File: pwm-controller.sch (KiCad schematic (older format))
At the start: 35 parts, among them J1 DEBUG_ADDRESS_I2C_INT, J2 POWER, J3 OUT+, J4 OUT-, SW1 EC12D1524403, U1 STM8S003F3Px, U2 78L05

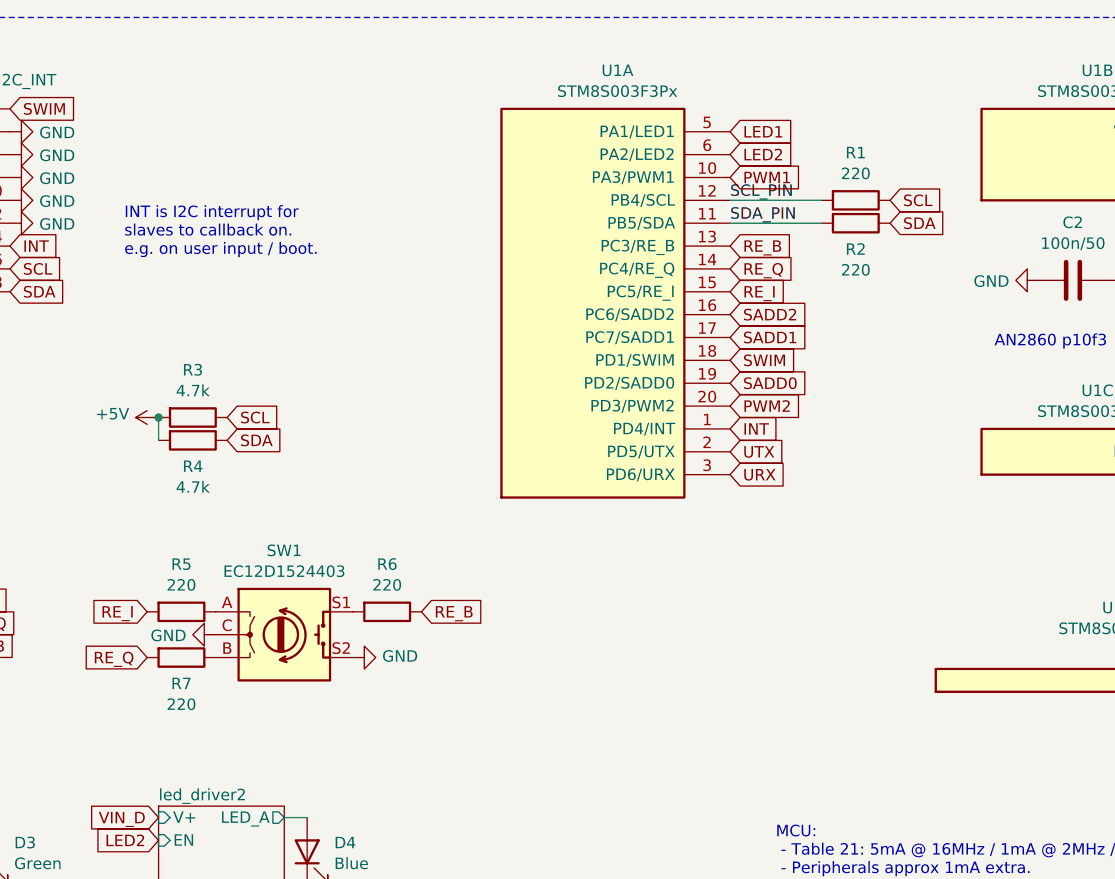
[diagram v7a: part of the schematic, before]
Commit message: add mosfets, fix led+i2c resistors
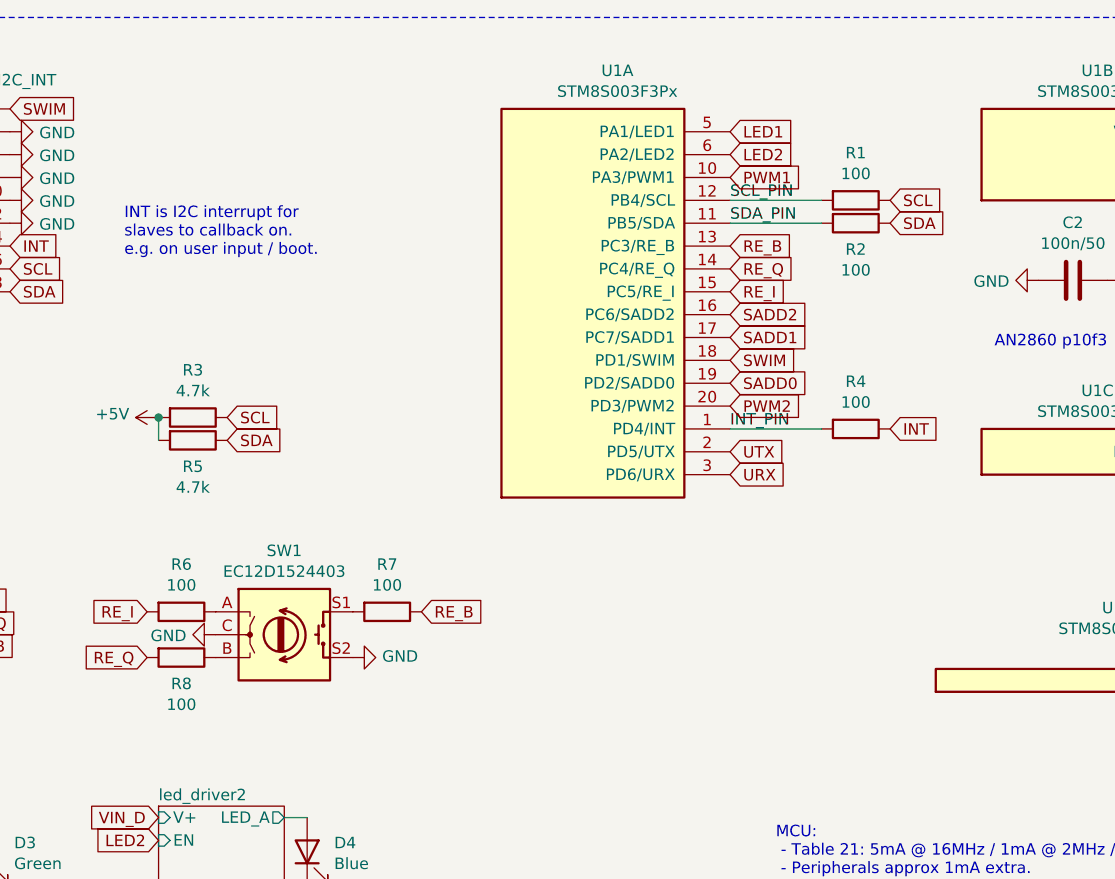
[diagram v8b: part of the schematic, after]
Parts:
- added R4: 100, Resistor_SMD:R_0402_1005Metric, symbol Device:R
- R1, R2: value 220 -> 100; JLC C25091 -> C25076
- R6: renamed from R5; value 220 -> 100; JLC C25091 -> C25076
- R7: renamed from R6; value 220 -> 100; JLC C25091 -> C25076
- R8: renamed from R7; value 220 -> 100; JLC C25091 -> C25076
- TP1: JLC (none) -> -
- renumbered R4 to R5
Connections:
- net INT: now also R4.1; no longer U1.1 (PD4/INT)
- new net INT_PIN: R4.2, U1.1 (PD4/INT)
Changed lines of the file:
@@
 AR Path="/61C031A1/61BB9F0D" Ref="R?"  Part="1"
 AR Path="/61C031A3/61BB9F0D" Ref="R?"  Part="1"
-AR Path="/61BB9F0D" Ref="R4"  Part="1"
-F 0 "R4" V 5915 3650 50  0000 C CNN
+AR Path="/61BB9F0D" Ref="R5"  Part="1"
+F 0 "R5" V 5915 3650 50  0000 C CNN
 F 1 "4.7k" V 6006 3650 50  0000 C CNN
 F 2 "Resistor_SMD:R_0402_1005Metric" V 5730 3650 50  0001 C CNN
@@
 Wire Wire Line
 	6200 6650 6200 6750
-Text GLabel 8150 3600 2    50   Input ~ 0
+Text GLabel 8850 3600 2    50   Input ~ 0
 INT
 Text GLabel 5000 2800 2    50   Input ~ 0
@@
 AR Path="/61C031A1/61CD939B" Ref="R?"  Part="1"
 AR Path="/61C031A3/61CD939B" Ref="R?"  Part="1"
-AR Path="/61CD939B" Ref="R5"  Part="1"
-F 0 "R5" V 5543 4400 50  0000 C CNN
-F 1 "220" V 5634 4400 50  0000 C CNN
+AR Path="/61CD939B" Ref="R6"  Part="1"
+F 0 "R6" V 5543 4400 50  0000 C CNN
+F 1 "100" V 5634 4400 50  0000 C CNN
 F 2 "Resistor_SMD:R_0402_1005Metric" V 5680 4400 50  0001 C CNN
 F 3 "~" H 5750 4400 50  0001 C CNN
-F 4 "C25091" H 5750 4400 50  0001 C CNN "JLC"
+F 4 "C25076" H 5750 4400 50  0001 C CNN "JLC"
 	1    5750 4400
 	0    1    1    0
@@
 AR Path="/61C031A1/61CD98C2" Ref="R?"  Part="1"
 AR Path="/61C031A3/61CD98C2" Ref="R?"  Part="1"
-AR Path="/61CD98C2" Ref="R7"  Part="1"
-F 0 "R7" V 5865 4600 50  0000 C CNN
-F 1 "220" V 5956 4600 50  0000 C CNN
+AR Path="/61CD98C2" Ref="R8"  Part="1"
+F 0 "R8" V 5865 4600 50  0000 C CNN
+F 1 "100" V 5956 4600 50  0000 C CNN
 F 2 "Resistor_SMD:R_0402_1005Metric" V 5680 4600 50  0001 C CNN
 F 3 "~" H 5750 4600 50  0001 C CNN
-F 4 "C25091" H 5750 4600 50  0001 C CNN "JLC"
+F 4 "C25076" H 5750 4600 50  0001 C CNN "JLC"
 	1    5750 4600
 	0    1    1    0
@@
 AR Path="/61C031A1/61CDA382" Ref="R?"  Part="1"
 AR Path="/61C031A3/61CDA382" Ref="R?"  Part="1"
-AR Path="/61CDA382" Ref="R6"  Part="1"
-F 0 "R6" V 6443 4400 50  0000 C CNN
-F 1 "220" V 6534 4400 50  0000 C CNN
+AR Path="/61CDA382" Ref="R7"  Part="1"
+F 0 "R7" V 6443 4400 50  0000 C CNN
+F 1 "100" V 6534 4400 50  0000 C CNN
 F 2 "Resistor_SMD:R_0402_1005Metric" V 6580 4400 50  0001 C CNN
 F 3 "~" H 6650 4400 50  0001 C CNN
-F 4 "C25091" H 6650 4400 50  0001 C CNN "JLC"
+F 4 "C25076" H 6650 4400 50  0001 C CNN "JLC"
 	1    6650 4400
 	0    1    1    0
@@
 AR Path="/61DB5806" Ref="R2"  Part="1"
 F 0 "R2" V 8815 2700 50  0000 C CNN
-F 1 "220" V 8906 2700 50  0000 C CNN
+F 1 "100" V 8906 2700 50  0000 C CNN
 F 2 "Resistor_SMD:R_0402_1005Metric" V 8630 2700 50  0001 C CNN
 F 3 "~" H 8700 2700 50  0001 C CNN
-F 4 "C25091" H 8700 2700 50  0001 C CNN "JLC"
+F 4 "C25076" H 8700 2700 50  0001 C CNN "JLC"
 	1    8700 2700
 	0    1    1    0
@@
 AR Path="/61DB4527" Ref="R1"  Part="1"
 F 0 "R1" V 8493 2600 50  0000 C CNN
-F 1 "220" V 8584 2600 50  0000 C CNN
+F 1 "100" V 8584 2600 50  0000 C CNN
 F 2 "Resistor_SMD:R_0402_1005Metric" V 8630 2600 50  0001 C CNN
 F 3 "~" H 8700 2600 50  0001 C CNN
-F 4 "C25091" H 8700 2600 50  0001 C CNN "JLC"
+F 4 "C25076" H 8700 2600 50  0001 C CNN "JLC"
 	1    8700 2600
 	0    1    1    0
@@
 F 2 "TestPoint:TestPoint_THTPad_D1.5mm_Drill0.7mm" H 2500 5300 50  0001 C CNN
 F 3 "~" H 2500 5300 50  0001 C CNN
+F 4 "-" H 2300 5300 50  0001 C CNN "JLC"
 	1    2300 5300
 	-1   0    0    1
 $EndComp
+$Comp
+L Device:R R?
+U 1 1 62317A5E
+P 8700 3600
+AR Path="/61B5C5B6/62317A5E" Ref="R?"  Part="1"
+AR Path="/61C03040/62317A5E" Ref="R?"  Part="1"
+AR Path="/61C031A1/62317A5E" Ref="R?"  Part="1"
+AR Path="/61C031A3/62317A5E" Ref="R?"  Part="1"
+AR Path="/62317A5E" Ref="R4"  Part="1"
+F 0 "R4" V 8493 3600 50  0000 C CNN
+F 1 "100" V 8584 3600 50  0000 C CNN
+F 2 "Resistor_SMD:R_0402_1005Metric" V 8630 3600 50  0001 C CNN
+F 3 "~" H 8700 3600 50  0001 C CNN
+F 4 "C25076" H 8700 3600 50  0001 C CNN "JLC"
+	1    8700 3600
+	0    1    1    0
+$EndComp
+Wire Wire Line
+	8550 3600 8150 3600
+Text Label 8150 3600 0    50   ~ 0
+INT_PIN
 $EndSCHEMATC
